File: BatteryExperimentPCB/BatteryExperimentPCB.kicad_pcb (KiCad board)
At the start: 2 copper layers, 27.8 x 32 mm, 32 parts, among them J1 USB_C_Receptacle_USB2.0_14P, J2 Conn_01x12_Pin, J3 Conn_01x12_Pin, Q1 DMG1012T, SW1 SW_Push, U1 ATtiny3226-M, U2 USBLC6-2P6, U3 BQ25628RYKR

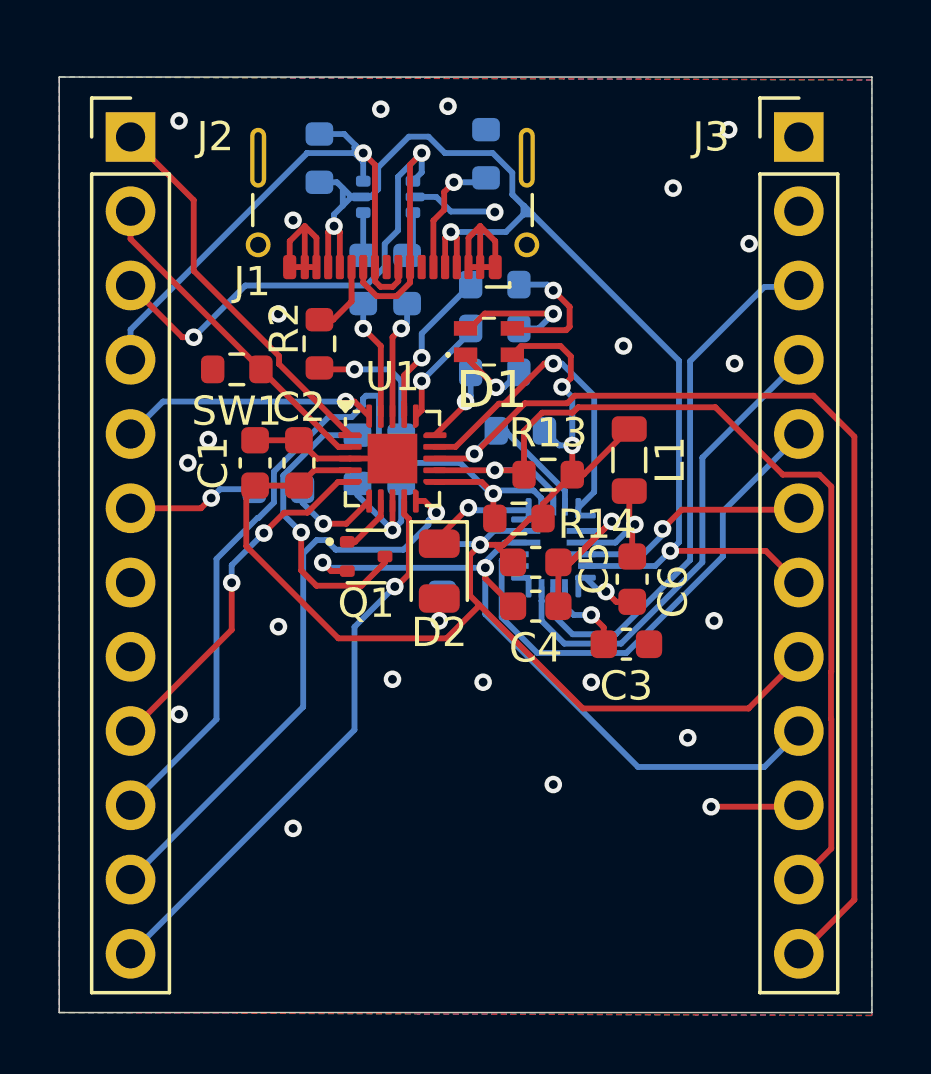
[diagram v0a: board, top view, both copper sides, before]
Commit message: redo pcb with components on single side, imported usb rohan uses
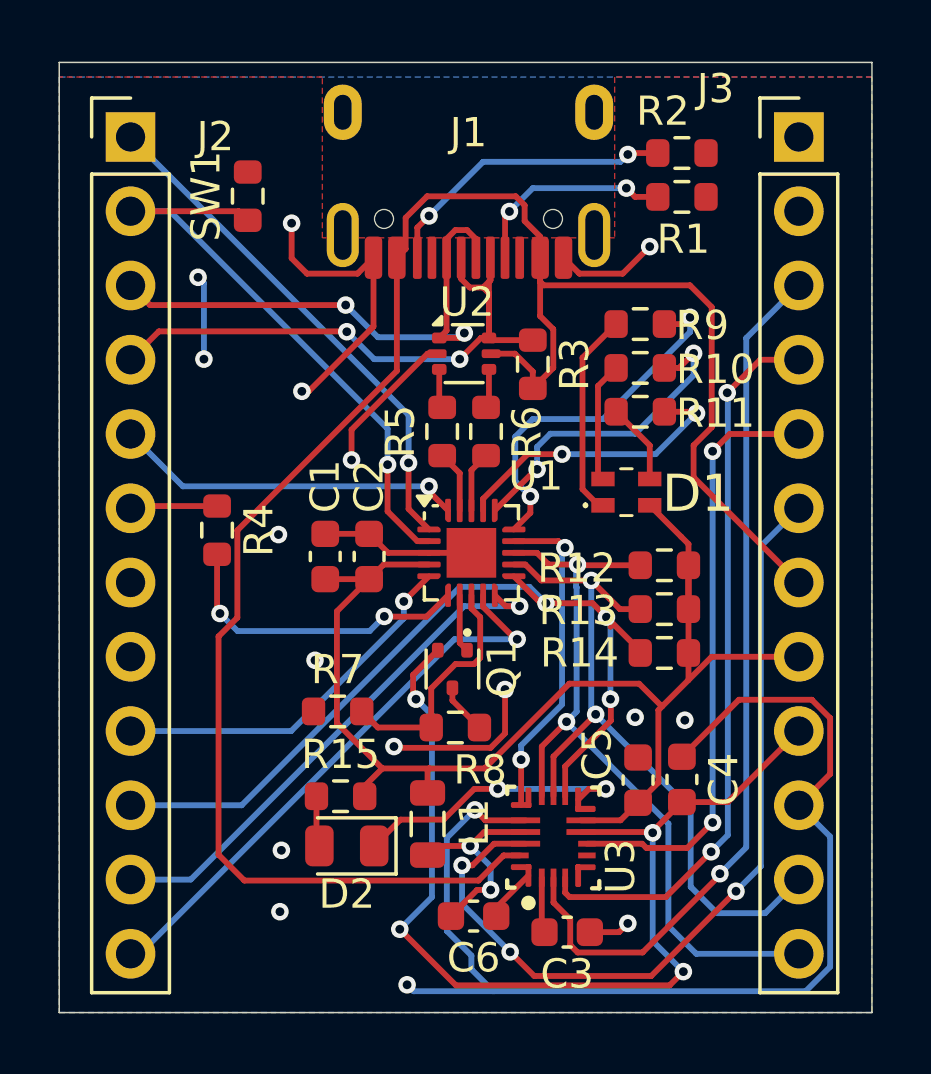
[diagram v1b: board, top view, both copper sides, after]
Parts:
- J1: value USB_C_Receptacle_USB2.0_14P -> TYPE-C-31-M-12; footprint Connector_USB:USB_C_Receptacle_G-Switch_GT-USB-7025 -> BatteryExperimentPCB:USB_C_Receptacle_Hroparts_TYPE-C-31-M-12
- R1, R10, R11, R12, R15, R3, R4, R5, R6, R7, R8, R9, U2, U3: moved to F.Cu
- moved L1 14.2 mm to (221.8, 80.5)
- moved R2 14.0 mm to (230.5, 57.5), turned to 0 degrees
- moved C6 12.7 mm to (223.4, 83.7), turned to 180 degrees
- moved R3 10.1 mm to (225.4, 64.8)
- moved C3 10.1 mm to (226.6, 84.2)
- moved D2 9.92 mm to (219.0, 81.2), turned to 180 degrees
- moved U3 9.90 mm to (226.1, 80.9)
- moved R8 9.77 mm to (222.8, 77.2), turned to 180 degrees
- moved R7 8.90 mm to (218.7, 76.7), turned to 0 degrees
- moved R15 8.54 mm to (218.8, 79.5), turned to 0 degrees
- moved C5 8.23 mm to (229.0, 79.0), turned to -90 degrees
- moved C4 7.75 mm to (230.5, 79.0), turned to -90 degrees
- moved D1 6.97 mm to (228.6, 69.2)
- moved R1 6.86 mm to (230.5, 59.0), turned to 0 degrees
- moved R14 6.78 mm to (229.9, 74.7)
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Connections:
- J1 pad A8: (no net) -> unconnected-(J1-SBU1-PadA8)
- J1 pad B8: (no net) -> unconnected-(J1-SBU2-PadB8)
- U1 pad 18: D+ -> D-
- U1 pad 19: D- -> D+
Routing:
- net GND: track 34.0 -> 73.5 mm, vias 25 -> 17
- net VBUS: track 42.7 -> 67.4 mm, vias 3 -> 0
- net PMID: track 8.20 -> 29.2 mm, vias 1 -> 3
- net SCL: track 39.6 -> 26.2 mm, vias 1 -> 2
- net PMID_GO: track 18.5 -> 30.2 mm, vias 0 -> 1
- net Battery+: track 25.1 -> 35.5 mm, vias 2 -> 4
- net CaseRed: track 2.66 -> 12.6 mm, vias 1 -> 2
- net Button: track 11.4 -> 20.7 mm, vias 0 -> 1
- net ILIM: track 16.3 -> 25.2 mm, vias 0 -> 2
- net SDA: track 33.3 -> 24.8 mm, vias 1 -> 2
- net Net-(Q1-D): track 10.2 -> 1.74 mm, vias 1 -> 0
- net Net-(J1-CC2): track 2.53 -> 10.3 mm, vias 0 -> 2
- net CaseGreen: track 3.78 -> 11.1 mm, vias 1 -> 2
- net Net-(U1-PA5): track 3.36 -> 10.6 mm, vias 1 -> 2
- net +3.75V: track 49.6 -> 43.4 mm, vias 3 -> 0
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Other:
- board size 27.8 x 32 mm -> 27.8 x 32.5 mm

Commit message: improve ground connections
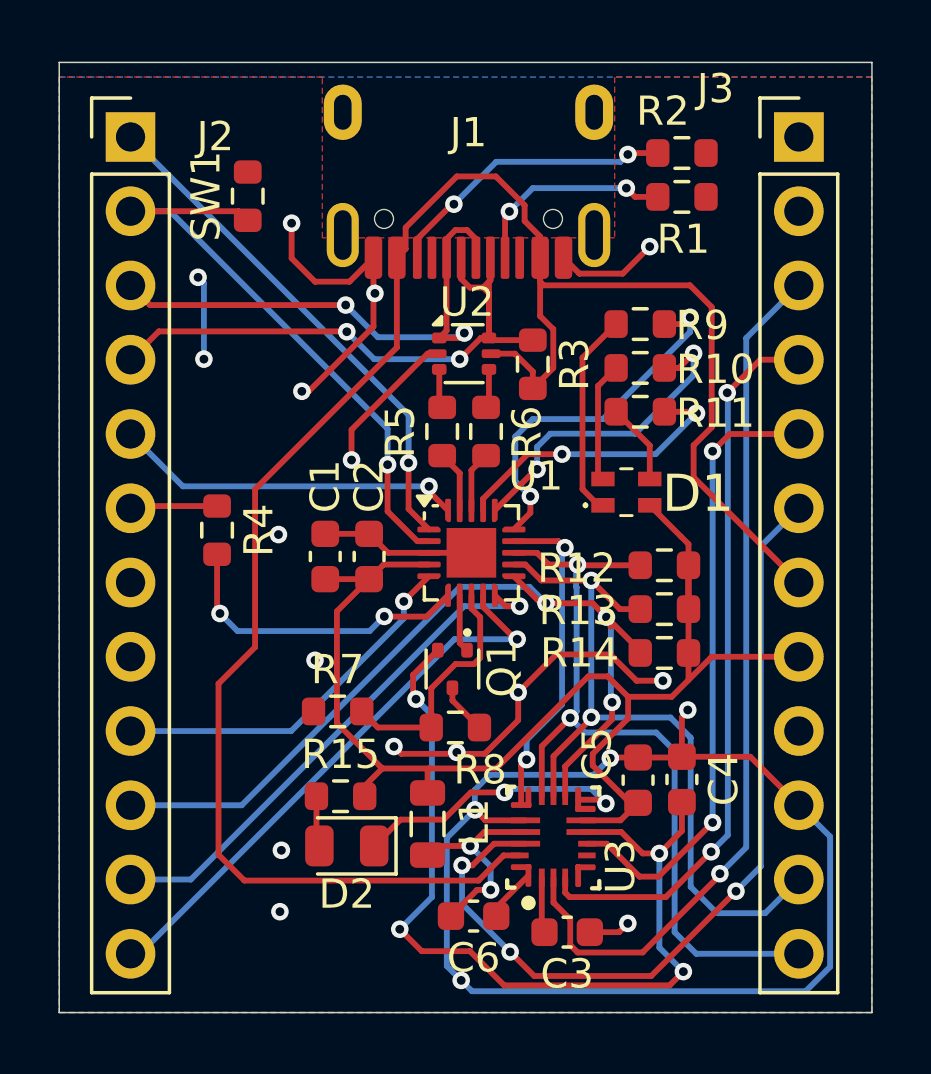
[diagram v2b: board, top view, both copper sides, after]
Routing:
- net GND: track 73.5 -> 82.5 mm, vias 17 -> 20
- net Battery+: track 35.5 -> 30.7 mm
- net SCL: track 26.2 -> 27.7 mm
- net SDA: track 24.8 -> 26.2 mm
- net +3.75V: track 43.4 -> 44.6 mm
- net QON: track 20.6 -> 21.4 mm

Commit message: connect unconnected item
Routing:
- net Battery+: track 30.7 -> 40.6 mm
- net GND: vias 20 -> 22
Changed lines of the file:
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@@
+	)
+	(via
+		(at 235.636337 81.299055)
+		(size 0.6)
+		(drill 0.3)
+		(layers "F.Cu" "B.Cu")
+		(free yes)
+		(net 1)
 	)
 	(via
@@
 		(drill 0.3)
 		(layers "F.Cu" "B.Cu")
+		(net 1)
+	)
+	(via
+		(at 235.7 76.1)
+		(size 0.6)
+		(drill 0.3)
+		(layers "F.Cu" "B.Cu")
+		(free yes)
 		(net 1)
 	)
@@
 	)
 	(segment
+		(start 233.8 81.1)
+		(end 235.1 81.1)
+		(width 0.2)
+		(layer "F.Cu")
+		(net 4)
+	)
+	(segment
 		(start 230.08 86.02)
 		(end 230.55 85.55)
@@
 	)
 	(segment
+		(start 232.45 79.75)
+		(end 233.8 81.1)
+		(width 0.2)
+		(layer "F.Cu")
+		(net 4)
+	)
+	(segment
 		(start 229.157304 81.507304)
 		(end 228.424998 80.774998)
@@
 	)
 	(segment
+		(start 235.1 81.1)
+		(end 235.9 80.3)
+		(width 0.2)
+		(layer "F.Cu")
+		(net 4)
+	)
+	(segment
 		(start 228.424998 80.774998)
 		(end 227.050001 80.774998)
@@
 	)
 	(segment
+		(start 235.9 78.72)
+		(end 234.5 77.32)
+		(width 0.2)
+		(layer "F.Cu")
+		(net 4)
+	)
+	(segment
 		(start 221.405 76.23039)
 		(end 221.305 76.13039)
@@
 	)
 	(segment
+		(start 235.9 80.3)
+		(end 235.9 78.72)
+		(width 0.2)
+		(layer "F.Cu")
+		(net 4)
+	)
+	(segment
 		(start 230.5 80.737304)
 		(end 229.73 81.507304)
@@
 		(width 0.2)
 		(layer "F.Cu")
+		(net 4)
+	)
+	(segment
+		(start 230.5 79.75)
+		(end 232.45 79.75)
+		(width 0.2)
+		(layer "F.Cu")
